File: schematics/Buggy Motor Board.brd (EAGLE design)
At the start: 100 x 80 mm, 48 parts, among them CON0 M025MM, CON1 M025MM, U2 MCP2562, U3 MCP2562, X1 MICROSD, X2 5566-24, X3 5566-24, Y1 16MHz

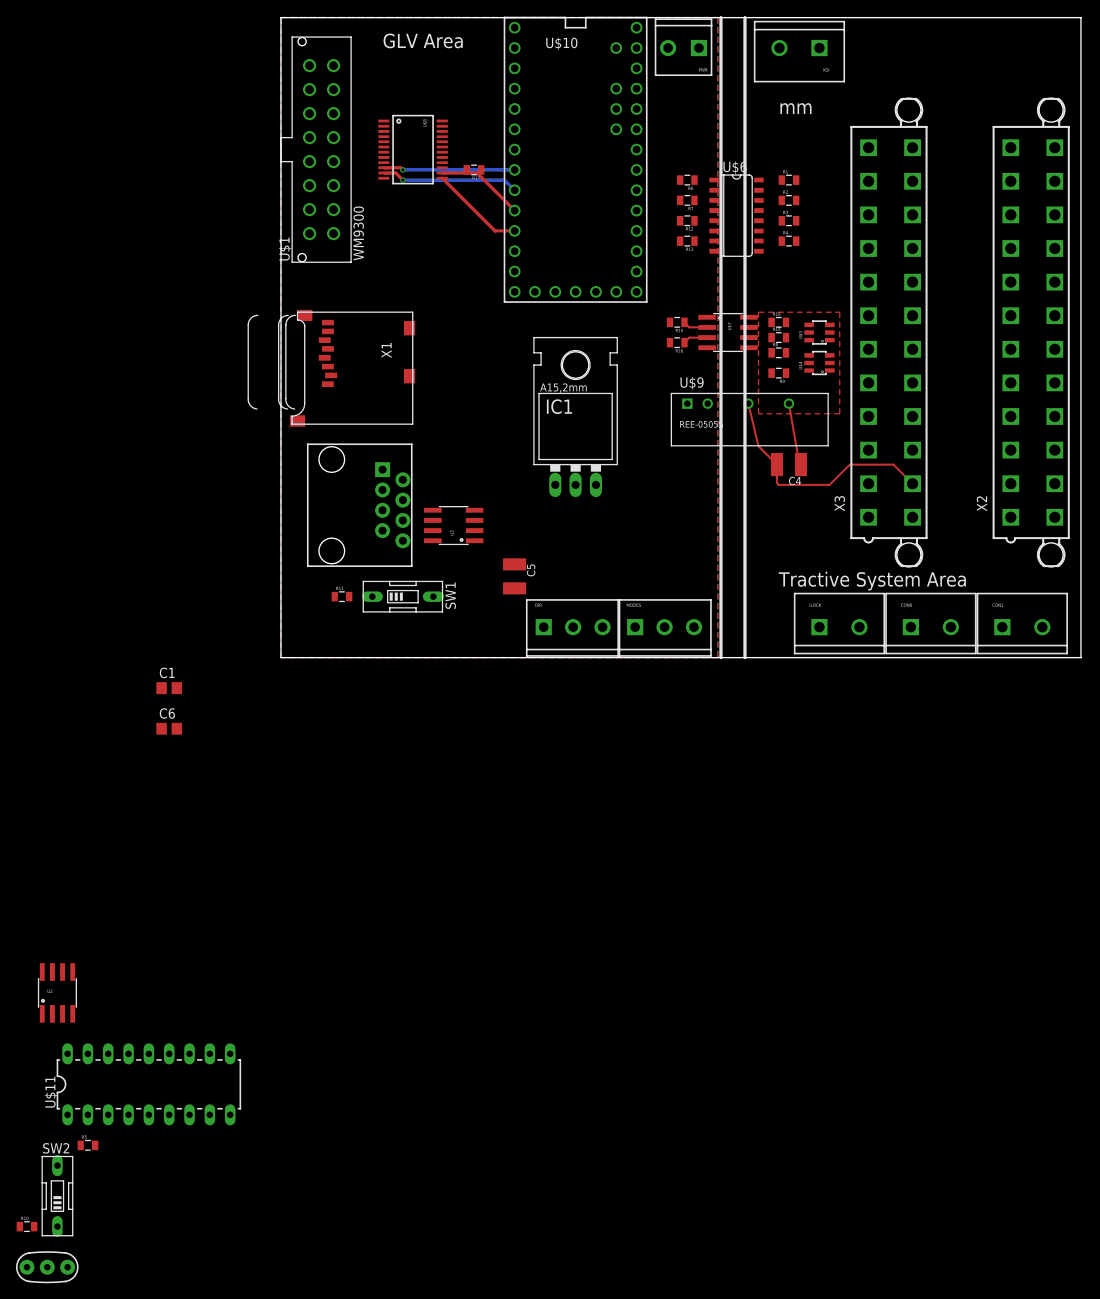
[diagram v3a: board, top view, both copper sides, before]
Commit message: Tested to be working with motors
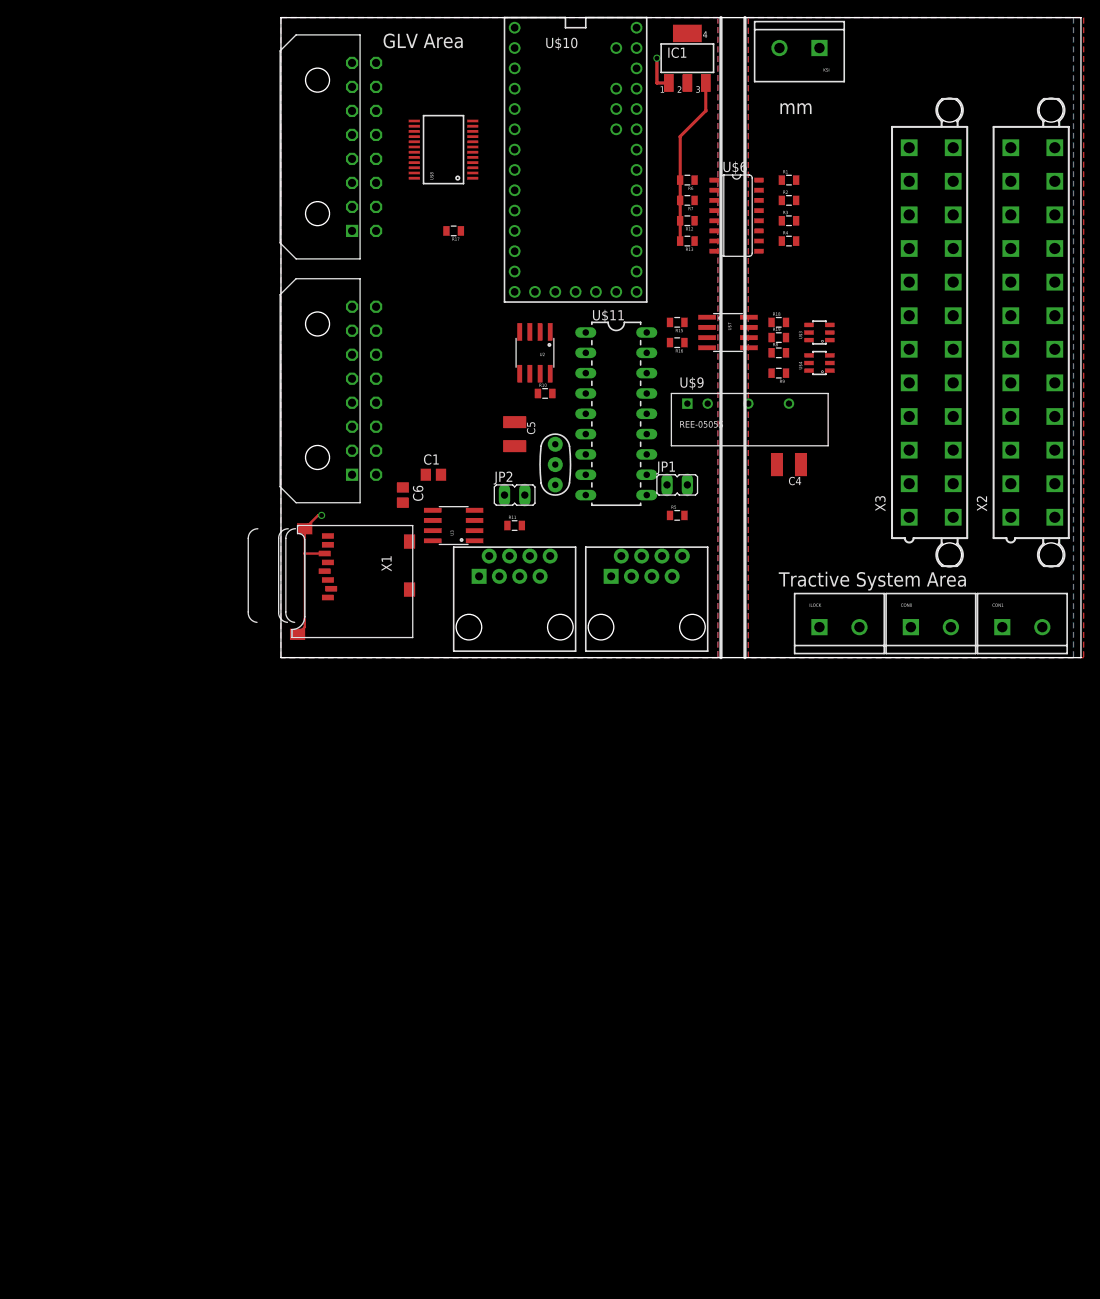
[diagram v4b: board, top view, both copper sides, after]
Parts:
- removed DIR, MODES: (no value), SparkFun-Connectors:SCREWTERMINAL-3.5MM-3_LOCK.007S
- removed PWR: M023.5MM_LOCK, SparkFun-Connectors:SCREWTERMINAL-3.5MM-2_LOCK
- removed SW1, SW2: (no value), special:EDG-01
- added JP1, JP2: (no value), jumper:JP1
- added U$12: 43045-1600, Wetmelon-Connectors:43045-1600
- added U$2: RJ45-8PTH, SparkFun-Connectors:RJ45-8
- IC1: value (none) -> 317EMP; device SparkFun-PowerIC:78XXL -> linear:SOT223
- U$1: value WM9300 -> 43045-1600; device Wetmelon-Connectors:WM9300 -> Wetmelon-Connectors:43045-1600
- moved R10 122.6 mm to (33.0, 33.0)
- moved Y1 118.7 mm to (34.3, 24.1), turned to 270 degrees
- moved R5 107.8 mm to (49.5, 17.8)
- moved U$11 102.2 mm to (41.9, 30.5), turned to 270 degrees
- moved U2 99.8 mm to (31.8, 38.1), turned to 180 degrees
- moved IC1 51.5 mm to (50.8, 74.9)
- moved C1 42.4 mm to (19.1, 22.9)
- moved C6 41.3 mm to (15.2, 20.3), turned to 270 degrees
- moved U$5 27.5 mm to (29.2, 3.81), turned to 0 degrees
- moved X1 26.7 mm to (16.5, 16.5)
- moved R11 23.3 mm to (29.2, 16.5)
- moved C5 17.8 mm to (29.2, 27.9)
- moved U$1 10.9 mm to (8.89, 53.3), turned to 270 degrees
- moved R17 8.03 mm to (21.6, 53.3)
- moved X3 5.08 mm to (81.3, 40.6)
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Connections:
- removed net CANH_HS: SW1.2, U$5.8, U3.7
- removed net CANH_LS: SW2.2, U$5.5, U2.7
- removed net CANL_HS: R11.1, U$5.7, U3.6
- removed net CANL_LS: R5.1, U$5.4, U2.6
- new net CANH0: JP2.1, U$2.8, U$5.8, U3.7
- new net CANH1: JP1.1, U$2.5, U$5.5, U2.7
- new net CANL0: R11.1, U$2.7, U$5.7, U3.6
- new net CANL1: R5.1, U$2.4, U$5.4, U2.6
- net +12V: now also IC1.3, U$12.11; no longer IC1.IN, PWR.2
- net +5V: now also IC1.4, U$12.10, U$12.9; no longer IC1.OUT
- net ENC0_A: now also U$12.1
- net ENC0_B: now also U$12.2
- net ENC0_Z: now also U$12.3
- net ENC1_A: now also U$12.4
- net ENC1_B: now also U$12.5
- net ENC1_Z: now also U$12.6
- net GND: now also IC1.1, U$12.16, U$12.7, U$12.8, U$2.1, U$2.2, U$2.3, U$2.6; no longer DIR.1, IC1.GND, MODES.1, PWR.1
- net N$1: now also JP1.2; no longer SW2.1
- net N$13: now also JP2.2; no longer SW1.1
- net OPTO0: now also U$12.12; no longer MODES.3
- net OPTO1: now also U$12.13; no longer MODES.2
- net OPTO2: now also U$12.14; no longer DIR.3
- net OPTO3: now also U$12.15; no longer DIR.2
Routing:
- net GND1: track 30.1 -> 0.00 mm
- net GND: track 0.00 -> 23.5 mm, vias 0 -> 2
- net +12V: track 0.00 -> 21.1 mm
- net AMUX1: track 17.2 -> 0.00 mm, vias 1 -> 0
- net AMUX0: track 16.5 -> 0.00 mm, vias 1 -> 0
- net AMUX3: track 11.8 -> 0.00 mm
- net AMUX2: track 11.0 -> 0.00 mm
- net +5V/1: track 7.82 -> 0.00 mm
- net SCL: track 3.10 -> 0.00 mm
- net SDA: track 3.10 -> 0.00 mm
- added copper zone on layer 1, net +5V
- added copper zone on layer 1, net GND1
- added copper zone on layer 16, net KSI
- removed copper zone on layer 1, net +5V/1
- removed copper zone on layer 1, net GND
